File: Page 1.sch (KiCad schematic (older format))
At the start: 33 parts

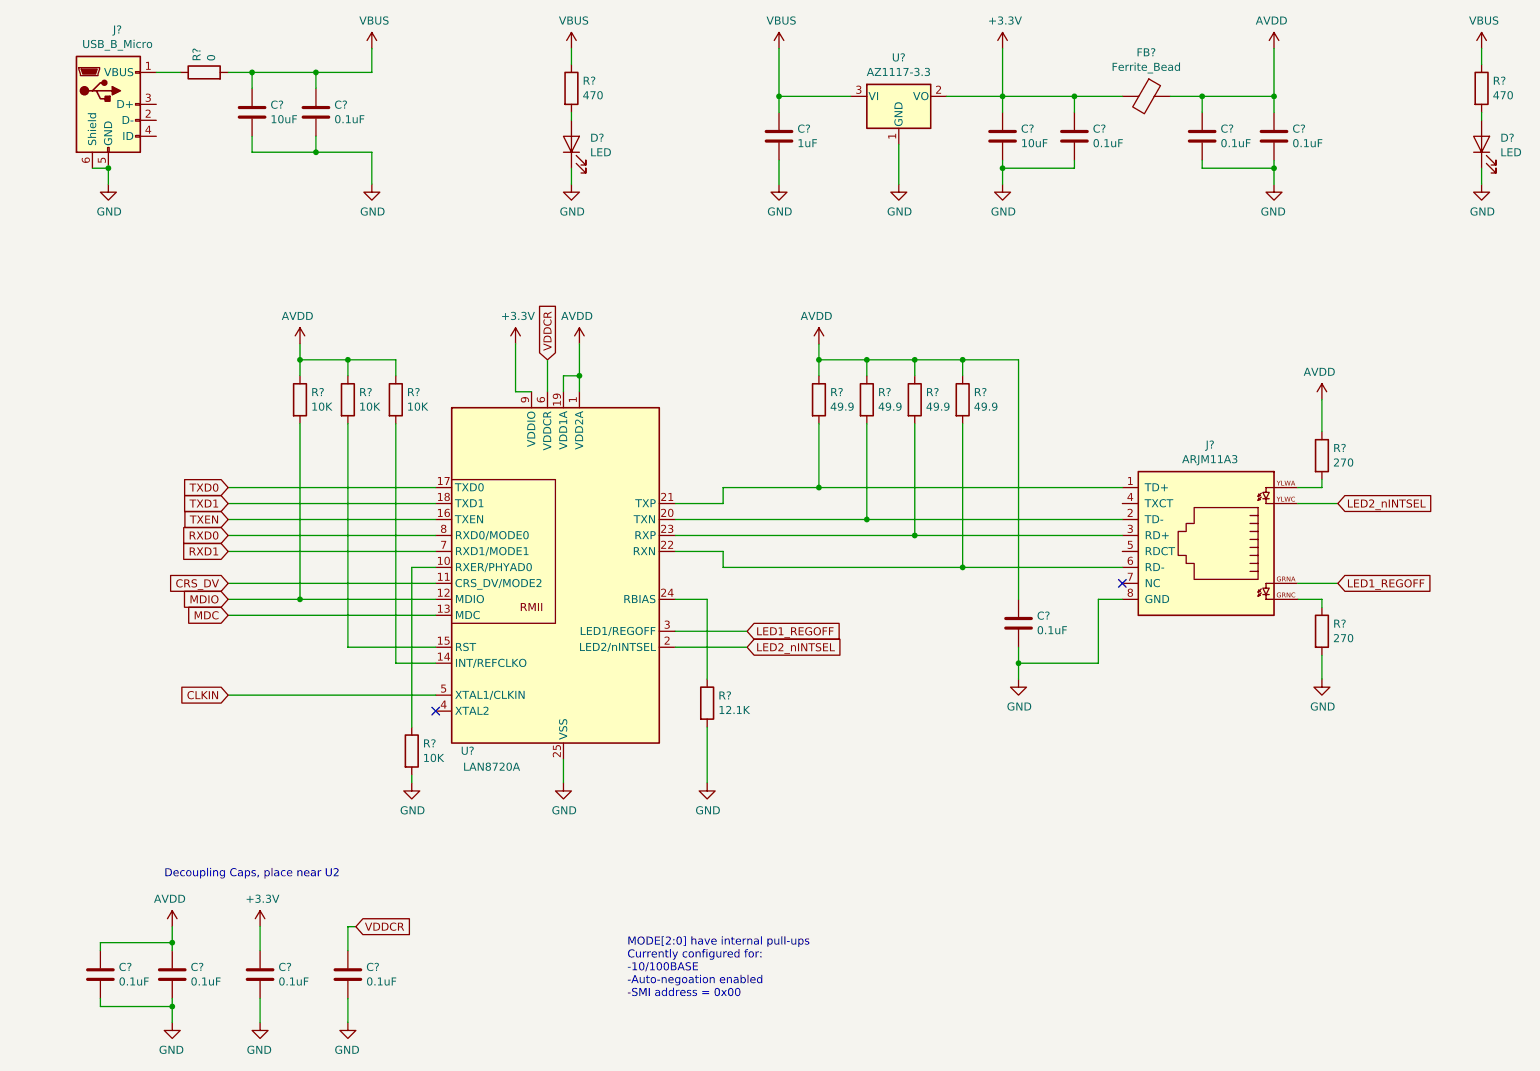
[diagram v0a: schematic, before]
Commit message: Corrected mistakes, added refdes
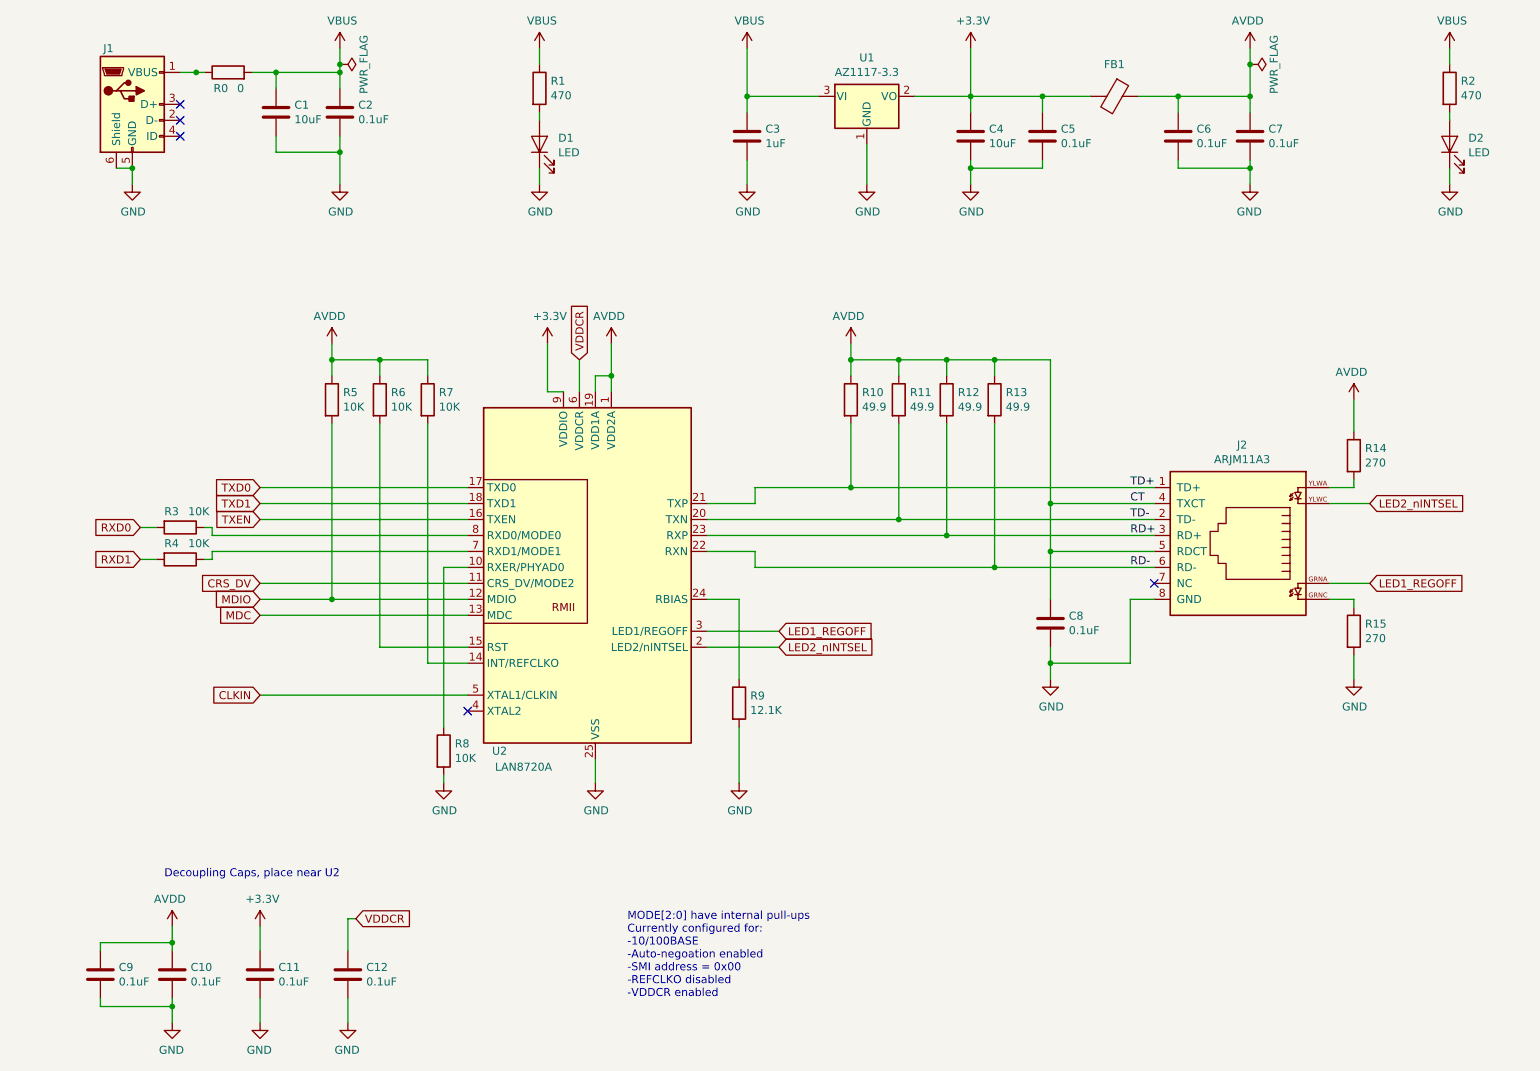
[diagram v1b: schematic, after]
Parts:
- added R3, R4: 10K, symbol Device:R
- gave numbers to parts that had none: 33
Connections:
- net AVDD: now also J2.4 (TXCT), J2.5 (RDCT)
- net RXD0: now also R3.2; no longer U2.8 (RXD0/MODE0)
- net RXD1: now also R4.2; no longer U2.7 (RXD1/MODE1)
- net TD-: now reaches J2.2 (TD-), R11.2, U2.20 (TXN)
- net TD+: now reaches J2.1 (TD+), R10.2, U2.21 (TXP)
- net RD-: now reaches J2.6 (RD-), R13.2, U2.22 (RXN)
- net RD+: now reaches J2.3 (RD+), R12.2, U2.23 (RXP)
- new net: R4.1, U2.7 (RXD1/MODE1)
- new net: R3.1, U2.8 (RXD0/MODE0)
- no-connect marks 2 -> 5
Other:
- note added: "MODE[2:0] have internal pull-ups\nCurrently configured for:\n-10/100BASE\n-Auto-negoation enabled\n-SMI address = 0x00\n-REFCLKO disabled\n-VDDCR enabled"
- note removed: "MODE[2:0] have internal pull-ups\nCurrently configured for:\n-10/100BASE\n-Auto-negoation enabled\n-SMI address = 0x00"
- moved on the sheet: C1, C2, C3, C4, C5, C6, C7, C8, D1, D2, FB1, J1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

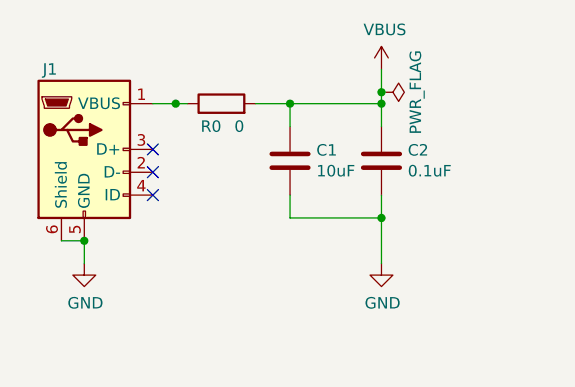
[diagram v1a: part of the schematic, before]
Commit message: Started assigning footprints
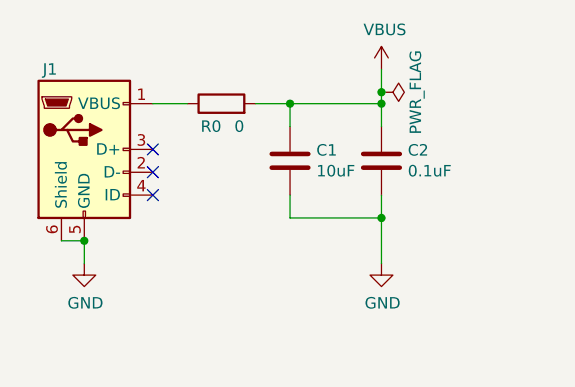
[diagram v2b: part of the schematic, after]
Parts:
- C1, C10, C11, C12, C2, C3, C4, C5, C6, C7, C8, C9: footprint (none) -> Capacitor_SMD:C_0603_1608Metric
- D1, D2: footprint (none) -> Diode_SMD:D_0603_1608Metric
- FB1: footprint (none) -> Inductor_SMD:L_0603_1608Metric
- J2: footprint ARJM11A3 -> (none)
- R0, R1, R10, R11, R12, R13, R14, R15, R2, R3, R4, R5, R6, R7, R8, R9: footprint (none) -> Resistor_SMD:R_0603_1608Metric
- U1: footprint (none) -> Package_TO_SOT_SMD:SOT-223
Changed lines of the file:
@@
 F 0 "C1" H 2765 1696 50  0000 L CNN
 F 1 "10uF" H 2765 1605 50  0000 L CNN
-F 2 "" H 2688 1500 50  0001 C CNN
+F 2 "Capacitor_SMD:C_0603_1608Metric" H 2688 1500 50  0001 C CNN
 F 3 "~" H 2650 1650 50  0001 C CNN
 	1    2650 1650
@@
 F 0 "C2" H 3165 1696 50  0000 L CNN
 F 1 "0.1uF" H 3165 1605 50  0000 L CNN
-F 2 "" H 3088 1500 50  0001 C CNN
+F 2 "Capacitor_SMD:C_0603_1608Metric" H 3088 1500 50  0001 C CNN
 F 3 "~" H 3050 1650 50  0001 C CNN
 	1    3050 1650
@@
 F 0 "R1" H 4370 1546 50  0000 L CNN
 F 1 "470" H 4370 1455 50  0000 L CNN
-F 2 "" V 4230 1500 50  0001 C CNN
+F 2 "Resistor_SMD:R_0603_1608Metric" V 4230 1500 50  0001 C CNN
 F 3 "~" H 4300 1500 50  0001 C CNN
 	1    4300 1500
@@
 F 0 "D1" V 4339 1733 50  0000 R CNN
 F 1 "LED" V 4248 1733 50  0000 R CNN
-F 2 "" H 4300 1850 50  0001 C CNN
+F 2 "Diode_SMD:D_0603_1608Metric" H 4300 1850 50  0001 C CNN
 F 3 "~" H 4300 1850 50  0001 C CNN
 	1    4300 1850
@@
 F 0 "U1" H 6350 1792 50  0000 C CNN
 F 1 "AZ1117-3.3" H 6350 1701 50  0000 C CNN
-F 2 "" H 6350 1800 50  0001 C CIN
+F 2 "Package_TO_SOT_SMD:SOT-223" H 6350 1800 50  0001 C CIN
 F 3 "https://www.diodes.com/assets/Datasheets/AZ1117.pdf" H 6350 1550 50  0001 C CNN
 	1    6350 1550
@@
 F 0 "C3" H 5715 1846 50  0000 L CNN
 F 1 "1uF" H 5715 1755 50  0000 L CNN
-F 2 "" H 5638 1650 50  0001 C CNN
+F 2 "Capacitor_SMD:C_0603_1608Metric" H 5638 1650 50  0001 C CNN
 F 3 "~" H 5600 1800 50  0001 C CNN
 	1    5600 1800
@@
 F 0 "FB1" V 7700 1550 50  0000 C CNN
 F 1 "Ferrite_Bead" V 7717 1550 50  0001 C CNN
-F 2 "" V 7830 1550 50  0001 C CNN
+F 2 "Inductor_SMD:L_0603_1608Metric" V 7830 1550 50  0001 C CNN
 F 3 "~" H 7900 1550 50  0001 C CNN
 	1    7900 1550
@@
 F 0 "C4" H 7115 1846 50  0000 L CNN
 F 1 "10uF" H 7115 1755 50  0000 L CNN
-F 2 "" H 7038 1650 50  0001 C CNN
+F 2 "Capacitor_SMD:C_0603_1608Metric" H 7038 1650 50  0001 C CNN
 F 3 "~" H 7000 1800 50  0001 C CNN
 	1    7000 1800
@@
 F 0 "C5" H 7565 1846 50  0000 L CNN
 F 1 "0.1uF" H 7565 1755 50  0000 L CNN
-F 2 "" H 7488 1650 50  0001 C CNN
+F 2 "Capacitor_SMD:C_0603_1608Metric" H 7488 1650 50  0001 C CNN
 F 3 "~" H 7450 1800 50  0001 C CNN
 	1    7450 1800
@@
 F 0 "R2" H 10070 1546 50  0000 L CNN
 F 1 "470" H 10070 1455 50  0000 L CNN
-F 2 "" V 9930 1500 50  0001 C CNN
+F 2 "Resistor_SMD:R_0603_1608Metric" V 9930 1500 50  0001 C CNN
 F 3 "~" H 10000 1500 50  0001 C CNN
 	1    10000 1500
@@
 F 0 "D2" V 10039 1733 50  0000 R CNN
 F 1 "LED" V 9948 1733 50  0000 R CNN
-F 2 "" H 10000 1850 50  0001 C CNN
+F 2 "Diode_SMD:D_0603_1608Metric" H 10000 1850 50  0001 C CNN
 F 3 "~" H 10000 1850 50  0001 C CNN
 	1    10000 1850
@@
 F 0 "J2" H 8700 5667 50  0000 C CNN
 F 1 "ARJM11A3" H 8700 5576 50  0000 C CNN
-F 2 "ARJM11A3" H 8250 4500 50  0001 L BNN
+F 2 "" H 8250 4500 50  0001 L BNN
 F 3 "" H 8250 4500 50  0001 C CNN
 	1    8750 4700
@@
 F 0 "R11" H 6620 3496 50  0000 L CNN
 F 1 "49.9" H 6620 3405 50  0000 L CNN
-F 2 "" V 6480 3450 50  0001 C CNN
+F 2 "Resistor_SMD:R_0603_1608Metric" V 6480 3450 50  0001 C CNN
 F 3 "~" H 6550 3450 50  0001 C CNN
 	1    6550 3450
@@
 F 0 "R12" H 6920 3496 50  0000 L CNN
 F 1 "49.9" H 6920 3405 50  0000 L CNN
-F 2 "" V 6780 3450 50  0001 C CNN
+F 2 "Resistor_SMD:R_0603_1608Metric" V 6780 3450 50  0001 C CNN
 F 3 "~" H 6850 3450 50  0001 C CNN
 	1    6850 3450
@@
 F 0 "R10" H 6320 3496 50  0000 L CNN
 F 1 "49.9" H 6320 3405 50  0000 L CNN
-F 2 "" V 6180 3450 50  0001 C CNN
+F 2 "Resistor_SMD:R_0603_1608Metric" V 6180 3450 50  0001 C CNN
 F 3 "~" H 6250 3450 50  0001 C CNN
 	1    6250 3450
@@
 F 0 "R14" H 9470 3846 50  0000 L CNN
 F 1 "270" H 9470 3755 50  0000 L CNN
-F 2 "" V 9330 3800 50  0001 C CNN
+F 2 "Resistor_SMD:R_0603_1608Metric" V 9330 3800 50  0001 C CNN
 F 3 "~" H 9400 3800 50  0001 C CNN
 	1    9400 3800
@@
 F 0 "R15" H 9470 4946 50  0000 L CNN
 F 1 "270" H 9470 4855 50  0000 L CNN
-F 2 "" V 9330 4900 50  0001 C CNN
+F 2 "Resistor_SMD:R_0603_1608Metric" V 9330 4900 50  0001 C CNN
 F 3 "~" H 9400 4900 50  0001 C CNN
 	1    9400 4900
@@
 F 0 "C8" H 7385 4896 50  0000 R CNN
 F 1 "0.1uF" H 7385 4805 50  0000 R CNN
-F 2 "" H 7538 4700 50  0001 C CNN
+F 2 "Capacitor_SMD:C_0603_1608Metric" H 7538 4700 50  0001 C CNN
 F 3 "~" H 7500 4850 50  0001 C CNN
 	1    7500 4850
@@
 F 0 "R9" H 5620 5396 50  0000 L CNN
 F 1 "12.1K" H 5620 5305 50  0000 L CNN
-F 2 "" V 5480 5350 50  0001 C CNN
+F 2 "Resistor_SMD:R_0603_1608Metric" V 5480 5350 50  0001 C CNN
 F 3 "~" H 5550 5350 50  0001 C CNN
 	1    5550 5350
@@
 F 0 "R8" H 3770 5696 50  0000 L CNN
 F 1 "10K" H 3770 5605 50  0000 L CNN
-F 2 "" V 3630 5650 50  0001 C CNN
+F 2 "Resistor_SMD:R_0603_1608Metric" V 3630 5650 50  0001 C CNN
 F 3 "~" H 3700 5650 50  0001 C CNN
 	1    3700 5650
@@
 F 0 "R13" H 7220 3496 50  0000 L CNN
 F 1 "49.9" H 7220 3405 50  0000 L CNN
-F 2 "" V 7080 3450 50  0001 C CNN
+F 2 "Resistor_SMD:R_0603_1608Metric" V 7080 3450 50  0001 C CNN
 F 3 "~" H 7150 3450 50  0001 C CNN
 	1    7150 3450
@@
 F 0 "C7" H 8635 1846 50  0000 R CNN
 F 1 "0.1uF" H 8635 1755 50  0000 R CNN
-F 2 "" H 8788 1650 50  0001 C CNN
+F 2 "Capacitor_SMD:C_0603_1608Metric" H 8788 1650 50  0001 C CNN
 F 3 "~" H 8750 1800 50  0001 C CNN
 	1    8750 1800
@@
 F 0 "C6" H 8185 1846 50  0000 R CNN
 F 1 "0.1uF" H 8185 1755 50  0000 R CNN
-F 2 "" H 8338 1650 50  0001 C CNN
+F 2 "Capacitor_SMD:C_0603_1608Metric" H 8338 1650 50  0001 C CNN
 F 3 "~" H 8300 1800 50  0001 C CNN
 	1    8300 1800
@@
 F 0 "R7" H 3670 3496 50  0000 L CNN
 F 1 "10K" H 3670 3405 50  0000 L CNN
-F 2 "" V 3530 3450 50  0001 C CNN
+F 2 "Resistor_SMD:R_0603_1608Metric" V 3530 3450 50  0001 C CNN
 F 3 "~" H 3600 3450 50  0001 C CNN
 	1    3600 3450
@@
 F 0 "R6" H 3370 3496 50  0000 L CNN
 F 1 "10K" H 3370 3405 50  0000 L CNN
-F 2 "" V 3230 3450 50  0001 C CNN
+F 2 "Resistor_SMD:R_0603_1608Metric" V 3230 3450 50  0001 C CNN
 F 3 "~" H 3300 3450 50  0001 C CNN
 	1    3300 3450
@@
 F 0 "R5" H 3070 3496 50  0000 L CNN
 F 1 "10K" H 3070 3405 50  0000 L CNN
-F 2 "" V 2930 3450 50  0001 C CNN
+F 2 "Resistor_SMD:R_0603_1608Metric" V 2930 3450 50  0001 C CNN
 F 3 "~" H 3000 3450 50  0001 C CNN
 	1    3000 3450
@@
 F 0 "R0" V 2250 1400 50  0000 L CNN
 F 1 "0" V 2250 1300 50  0000 L CNN
-F 2 "" V 2280 1400 50  0001 C CNN
+F 2 "Resistor_SMD:R_0603_1608Metric" V 2280 1400 50  0001 C CNN
 F 3 "~" H 2350 1400 50  0001 C CNN
 	1    2350 1400
 	0    -1   -1   0
 $EndComp
-Wire Wire Line
-	2050 1400 2150 1400
 Wire Wire Line
 	2500 1400 2650 1400
@@
 F 0 "C10" H 1885 7096 50  0000 R CNN
 F 1 "0.1uF" H 1885 7005 50  0000 R CNN
-F 2 "" H 2038 6900 50  0001 C CNN
+F 2 "Capacitor_SMD:C_0603_1608Metric" H 2038 6900 50  0001 C CNN
 F 3 "~" H 2000 7050 50  0001 C CNN
 	1    2000 7050
@@
 F 0 "C9" H 1435 7096 50  0000 R CNN
 F 1 "0.1uF" H 1435 7005 50  0000 R CNN
-F 2 "" H 1588 6900 50  0001 C CNN
+F 2 "Capacitor_SMD:C_0603_1608Metric" H 1588 6900 50  0001 C CNN
 F 3 "~" H 1550 7050 50  0001 C CNN
 	1    1550 7050
@@
 F 0 "C11" H 2435 7096 50  0000 R CNN
 F 1 "0.1uF" H 2435 7005 50  0000 R CNN
-F 2 "" H 2588 6900 50  0001 C CNN
+F 2 "Capacitor_SMD:C_0603_1608Metric" H 2588 6900 50  0001 C CNN
 F 3 "~" H 2550 7050 50  0001 C CNN
 	1    2550 7050
@@
 F 0 "C12" H 2985 7096 50  0000 R CNN
 F 1 "0.1uF" H 2985 7005 50  0000 R CNN
-F 2 "" H 3138 6900 50  0001 C CNN
+F 2 "Capacitor_SMD:C_0603_1608Metric" H 3138 6900 50  0001 C CNN
 F 3 "~" H 3100 7050 50  0001 C CNN
 	1    3100 7050
@@
 F 0 "R3" V 1950 4150 50  0000 L CNN
 F 1 "10K" V 1950 4300 50  0000 L CNN
-F 2 "" V 1980 4250 50  0001 C CNN
+F 2 "Resistor_SMD:R_0603_1608Metric" V 1980 4250 50  0001 C CNN
 F 3 "~" H 2050 4250 50  0001 C CNN
 	1    2050 4250
@@
 F 0 "R4" V 1950 4350 50  0000 L CNN
 F 1 "10K" V 1950 4500 50  0000 L CNN
-F 2 "" V 1980 4450 50  0001 C CNN
+F 2 "Resistor_SMD:R_0603_1608Metric" V 1980 4450 50  0001 C CNN
 F 3 "~" H 2050 4450 50  0001 C CNN
 	1    2050 4450
@@
 	0    1    1    0
 $EndComp
-Connection ~ 2150 1400
-Wire Wire Line
-	2150 1400 2200 1400
 Connection ~ 3050 1350
 Wire Wire Line
@@
 Text Label 8000 4500 0    50   ~ 0
 RD-
+Wire Wire Line
+	2050 1400 2200 1400
 $EndSCHEMATC

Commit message: Assigning footprints
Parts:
- removed J1: USB_B_Micro, symbol Connector:USB_B_Micro
- added J1: 10118192-0001LF, symbol Symbols:10118192-0001LF
- J2: footprint (none) -> kicad-library:ARJM11A3-009-AB-ER2-T
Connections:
- net GND: now also J1.5 (GND), J1.SH (Shield)
- net at R0.1: now also J1.1 (VBUS)
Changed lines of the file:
@@
 EESchema Schematic File Version 4
-LIBS:EsperDNS-cache
 EELAYER 30 0
 EELAYER END
@@
 $EndDescr
 $Comp
-L Connector:USB_B_Micro J?
-U 1 1 5DF04BA1
-P 1750 1600
-AR Path="/5DF04BA1" Ref="J?"  Part="1"
-AR Path="/5DED2F9B/5DF04BA1" Ref="J1"  Part="1"
-F 0 "J1" H 1600 1950 50  0000 C CNN
-F 1 "USB_B_Micro" H 1750 1950 50  0001 C CNN
-F 2 "" H 1900 1550 50  0001 C CNN
-F 3 "~" H 1900 1550 50  0001 C CNN
-	1    1750 1600
-	1    0    0    -1
-$EndComp
-$Comp
 L Device:C C?
 U 1 1 5DF04BA7
@@
 Wire Wire Line
 	1650 2000 1750 2000
-Connection ~ 1750 2000
 Wire Wire Line
 	3050 2100 3050 1900
@@
 F 0 "J2" H 8700 5667 50  0000 C CNN
 F 1 "ARJM11A3" H 8700 5576 50  0000 C CNN
-F 2 "" H 8250 4500 50  0001 L BNN
+F 2 "kicad-library:ARJM11A3-009-AB-ER2-T" H 8250 4500 50  0001 L BNN
 F 3 "" H 8250 4500 50  0001 C CNN
 	1    8750 4700
@@
 Wire Wire Line
 	2050 1400 2200 1400
+$Comp
+L Symbols:10118192-0001LF J1
+U 1 1 5DEC996C
+P 1750 1600
+F 0 "J1" H 1807 1975 50  0000 C CNN
+F 1 "10118192-0001LF" H 1807 1976 50  0001 C CNN
+F 2 "" H 1900 1550 50  0001 C CNN
+F 3 "~" H 1900 1550 50  0001 C CNN
+	1    1750 1600
+	1    0    0    -1
+$EndComp
+Connection ~ 1750 2000
 $EndSCHEMATC

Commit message: Started laying out board
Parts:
- removed C5, C7: 0.1uF, Capacitor_SMD:C_0603_1608Metric, symbol Device:C
- added C16, C17: 1uF, Capacitor_SMD:C_0603_1608Metric, symbol Device:C
- added R27: 10K, Resistor_SMD:R_0603_1608Metric, symbol Device:R
- C4: value 10uF -> 4.7uF
- C6: value 0.1uF -> 4.7uF
- J1: footprint (none) -> digikey-footprints:USB_Micro_B_Female_10118192; symbol Symbols:10118192-0001LF -> EsperDNS-rescue:10118192-0001LF-Symbols
- J2: footprint kicad-library:ARJM11A3-009-AB-ER2-T -> My Footprints:ARJM11A3-009-AB-ER2-T
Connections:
- net AVDD: now also C17.1
- net CRS_DV: now also R27.2; no longer U2.11 (CRS_DV/MODE2)
- net GND: now also C16.2, C17.2
- net VDDCR: now also C16.1
- new net: R27.1, U2.11 (CRS_DV/MODE2)
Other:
- note added: "MODE[2:0] have internal pull-ups\nCurrently configured for:\n-10/100BASE\n-Auto-negoation enabled\n-SMI address = 0x00\n-nINT enabled, REFCLKO disabled\n-VDDCR enabled"
- note removed: "MODE[2:0] have internal pull-ups\nCurrently configured for:\n-10/100BASE\n-Auto-negoation enabled\n-SMI address = 0x00\n-REFCLKO disabled\n-VDDCR enabled"
- moved on the sheet: C3, C4, C6, D1, FB1, R1, R8, U1
